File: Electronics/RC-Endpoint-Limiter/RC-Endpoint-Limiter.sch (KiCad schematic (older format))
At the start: 38 parts

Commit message: polished electornics
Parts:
- added J2: Aux Low, symbol Connector_Generic:Conn_01x03
- added J3: Aux High, symbol Connector_Generic:Conn_01x03
- added R7: 1K, symbol Device:R_Small
- added R8: 100R, symbol Device:R_Small
- R5: renamed from R?; value 240R -> 100R
- gave numbers to parts that had none: 37
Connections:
- net GND: now also J2.2 (Pin_2), J3.2 (Pin_2)
- net VCC: now also J2.1 (Pin_1), J3.1 (Pin_1)
- net at U1.11 (PB3): no longer R4.2
- net at U1.19 (PD1): now also R6.2
- net at U1.20 (PD2): now also R7.2
- net at U1.21 (PD3): now also R8.2
- net at U1.25 (PD4): now also R9.2
- net at U1.28 (PB4): now also J2.3 (Pin_3); no longer R6.2
- net at U1.29 (PB5): now also J3.3 (Pin_3); no longer R9.2
- net at U1.30 (PB6): now also R4.2
- net at D7.2 (A), J7.2 (Pin_2): now also JP1.1 (A); no longer JP1.2 (B)
- net at J7.3 (Pin_3), R5.1: now also R8.1
- net at D6.2 (A), J6.2 (Pin_2): now also JP1.2 (B); no longer JP1.1 (A)
- net at J6.3 (Pin_3), R9.1: now also R7.1
- no-connect marks 0 -> 15
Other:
- moved on the sheet: C1, C2, C3, C4, C5, C6, C7, D1, D2, D3, D4, D5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

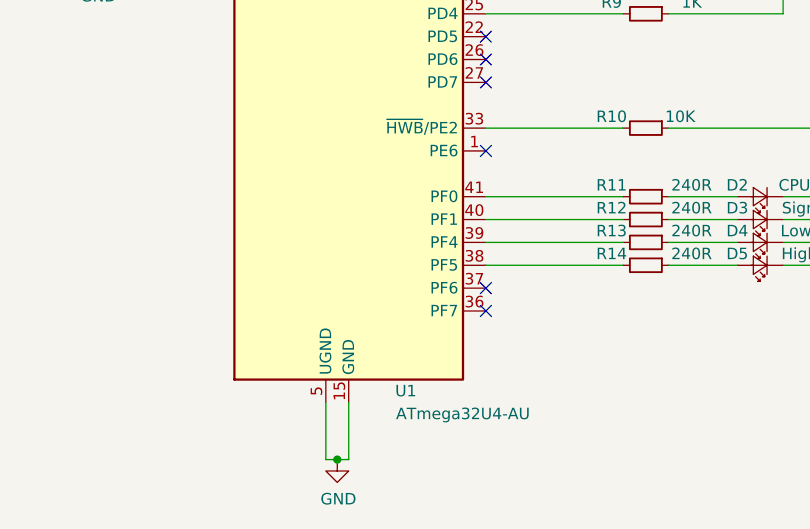
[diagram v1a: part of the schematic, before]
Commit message: started component assignment
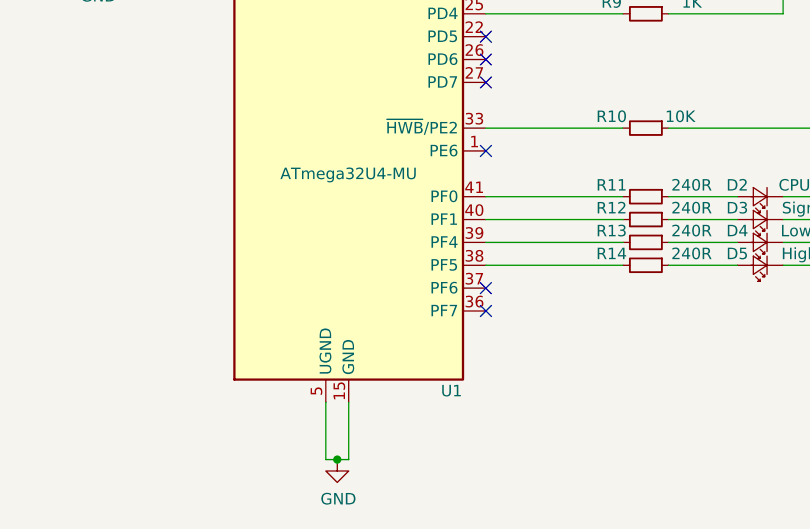
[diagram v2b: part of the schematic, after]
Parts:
- removed U1: ATmega32U4-AU, Package_QFP:TQFP-44_10x10mm_P0.8mm, symbol MCU_Microchip_ATmega:ATmega32U4-AU
- added U1: ATmega32U4-MU, Package_DFN_QFN:QFN-44-1EP_7x7mm_P0.5mm_EP5.2x5.2mm, symbol MCU_Microchip_ATmega:ATmega32U4-MU
- C1, C2, C3, C4, C5, C6, C7, R1, R10, R11, R12, R13, R14, R15, R16, R17, R18, R2, R3, R4, R5, R6, R7, R8, R9: footprint (none) -> Capacitor_SMD:C_0805_2012Metric
- J4, J5: footprint (none) -> Connector_AMASS:AMASS_MR30PW-FB_1x03_P3.50mm_Horizontal
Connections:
- net GND: now also U1.15 (GND), U1.23 (GND), U1.35 (GND), U1.43 (GND), U1.45 (GND), U1.5 (UGND)
- net VCC: now also U1.14 (VCC), U1.2 (UVCC), U1.24 (AVCC), U1.34 (VCC), U1.44 (AVCC)
- net at R3.1: now also U1.13 (~RESET)
- net at C2.2, Y1.2: now also U1.16 (XTAL2)
- net at C1.1, Y1.1: now also U1.17 (XTAL1)
- net at R6.2: now also U1.19 (PD1)
- net at R7.2: now also U1.20 (PD2)
- net at R8.2: now also U1.21 (PD3)
- net at R9.2: now also U1.25 (PD4)
- net at J2.3 (Pin_3): now also U1.28 (PB4)
- net at J3.3 (Pin_3): now also U1.29 (PB5)
- net at R2.1: now also U1.3 (D-)
- net at R4.2: now also U1.30 (PB6)
- net at R5.2: now also U1.31 (PC6)
- net at R10.2: now also U1.33 (~HWB~/PE2)
- net at R14.2: now also U1.38 (PF5)
- net at R13.2: now also U1.39 (PF4)
- net at R1.1: now also U1.4 (D+)
- net at R12.2: now also U1.40 (PF1)
- net at R11.2: now also U1.41 (PF0)
- net at C3.1: now also U1.42 (AREF)
- net at C4.1: now also U1.6 (UCAP)
- net at D1.2 (A), J1.1 (VBUS): now also U1.7 (VBUS)
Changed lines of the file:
@@
 EESchema Schematic File Version 4
 LIBS:RC-Endpoint-Limiter-cache
-EELAYER 30 0
+EELAYER 29 0
 EELAYER END
 $Descr A4 11693 8268
 encoding utf-8
 Sheet 1 1
-Title ""
-Date ""
-Rev ""
-Comp ""
+Title "RC Endpoint Limiter"
+Date "2019-09-01"
+Rev "0.01"
+Comp "Vapourforge"
 Comment1 ""
 Comment2 ""
@@
 F 0 "C1" V 2700 3000 50  0000 C CNN
 F 1 "22pf" V 2700 3300 50  0000 C CNN
-F 2 "" H 2750 3100 50  0001 C CNN
+F 2 "Capacitor_SMD:C_0805_2012Metric" H 2750 3100 50  0001 C CNN
 F 3 "~" H 2750 3100 50  0001 C CNN
 	1    2750 3100
@@
 F 0 "C2" V 2800 3400 50  0000 C CNN
 F 1 "22pf" V 2800 3100 50  0000 C CNN
-F 2 "" H 2750 3300 50  0001 C CNN
+F 2 "Capacitor_SMD:C_0805_2012Metric" H 2750 3300 50  0001 C CNN
 F 3 "~" H 2750 3300 50  0001 C CNN
 	1    2750 3300
@@
 F 0 "C3" V 2700 3400 50  0000 C CNN
 F 1 "100n" V 2700 3700 50  0000 C CNN
-F 2 "" H 2750 3500 50  0001 C CNN
+F 2 "Capacitor_SMD:C_0805_2012Metric" H 2750 3500 50  0001 C CNN
 F 3 "~" H 2750 3500 50  0001 C CNN
 	1    2750 3500
@@
 F 0 "R3" V 3150 2750 50  0000 C CNN
 F 1 "10K" V 3150 3050 50  0000 C CNN
-F 2 "" H 3200 2900 50  0001 C CNN
+F 2 "Capacitor_SMD:C_0805_2012Metric" H 3200 2900 50  0001 C CNN
 F 3 "~" H 3200 2900 50  0001 C CNN
 	1    3200 2900
@@
 F 0 "C7" V 4550 2350 50  0000 C CNN
 F 1 "1uF" V 4550 2650 50  0000 C CNN
-F 2 "" H 4600 2450 50  0001 C CNN
+F 2 "Capacitor_SMD:C_0805_2012Metric" H 4600 2450 50  0001 C CNN
 F 3 "~" H 4600 2450 50  0001 C CNN
 	1    4600 2450
@@
 F 0 "C6" V 4550 2200 50  0000 C CNN
 F 1 "1uF" V 4550 2500 50  0000 C CNN
-F 2 "" H 4600 2300 50  0001 C CNN
+F 2 "Capacitor_SMD:C_0805_2012Metric" H 4600 2300 50  0001 C CNN
 F 3 "~" H 4600 2300 50  0001 C CNN
 	1    4600 2300
@@
 F 0 "C5" V 4550 2050 50  0000 C CNN
 F 1 "1uF" V 4550 2350 50  0000 C CNN
-F 2 "" H 4600 2150 50  0001 C CNN
+F 2 "Capacitor_SMD:C_0805_2012Metric" H 4600 2150 50  0001 C CNN
 F 3 "~" H 4600 2150 50  0001 C CNN
 	1    4600 2150
@@
 F 0 "C4" V 3250 4100 50  0000 C CNN
 F 1 "1uF" V 3250 4400 50  0000 C CNN
-F 2 "" H 3300 4200 50  0001 C CNN
+F 2 "Capacitor_SMD:C_0805_2012Metric" H 3300 4200 50  0001 C CNN
 F 3 "~" H 3300 4200 50  0001 C CNN
 	1    3300 4200
@@
 F 0 "R1" V 2200 3750 50  0000 C CNN
 F 1 "22R" V 2200 4050 50  0000 C CNN
-F 2 "" H 2250 3900 50  0001 C CNN
+F 2 "Capacitor_SMD:C_0805_2012Metric" H 2250 3900 50  0001 C CNN
 F 3 "~" H 2250 3900 50  0001 C CNN
 	1    2250 3900
@@
 F 0 "R2" V 2200 3850 50  0000 C CNN
 F 1 "22R" V 2200 4150 50  0000 C CNN
-F 2 "" H 2250 4000 50  0001 C CNN
+F 2 "Capacitor_SMD:C_0805_2012Metric" H 2250 4000 50  0001 C CNN
 F 3 "~" H 2250 4000 50  0001 C CNN
 	1    2250 4000
@@
 F 0 "R11" V 5500 5150 50  0000 C CNN
 F 1 "240R" V 5500 5500 50  0000 C CNN
-F 2 "" H 5550 5300 50  0001 C CNN
+F 2 "Capacitor_SMD:C_0805_2012Metric" H 5550 5300 50  0001 C CNN
 F 3 "~" H 5550 5300 50  0001 C CNN
 	1    5550 5300
@@
 F 0 "R12" V 5500 5250 50  0000 C CNN
 F 1 "240R" V 5500 5600 50  0000 C CNN
-F 2 "" H 5550 5400 50  0001 C CNN
+F 2 "Capacitor_SMD:C_0805_2012Metric" H 5550 5400 50  0001 C CNN
 F 3 "~" H 5550 5400 50  0001 C CNN
 	1    5550 5400
@@
 F 0 "R13" V 5500 5350 50  0000 C CNN
 F 1 "240R" V 5500 5700 50  0000 C CNN
-F 2 "" H 5550 5500 50  0001 C CNN
+F 2 "Capacitor_SMD:C_0805_2012Metric" H 5550 5500 50  0001 C CNN
 F 3 "~" H 5550 5500 50  0001 C CNN
 	1    5550 5500
@@
 F 0 "R14" V 5500 5450 50  0000 C CNN
 F 1 "240R" V 5500 5800 50  0000 C CNN
-F 2 "" H 5550 5600 50  0001 C CNN
+F 2 "Capacitor_SMD:C_0805_2012Metric" H 5550 5600 50  0001 C CNN
 F 3 "~" H 5550 5600 50  0001 C CNN
 	1    5550 5600
@@
 F 0 "R10" V 5500 4850 50  0000 C CNN
 F 1 "10K" V 5500 5150 50  0000 C CNN
-F 2 "" H 5550 5000 50  0001 C CNN
+F 2 "Capacitor_SMD:C_0805_2012Metric" H 5550 5000 50  0001 C CNN
 F 3 "~" H 5550 5000 50  0001 C CNN
 	1    5550 5000
@@
 F 0 "J4" V 7288 2112 50  0000 R CNN
 F 1 "Switch Low" V 7400 2450 50  0000 R CNN
-F 2 "" H 7350 2300 50  0001 C CNN
+F 2 "Connector_AMASS:AMASS_MR30PW-FB_1x03_P3.50mm_Horizontal" H 7350 2300 50  0001 C CNN
 F 3 "~" H 7350 2300 50  0001 C CNN
 	1    7350 2300
@@
 F 0 "J5" V 8238 2112 50  0000 R CNN
 F 1 "Switch High" V 8350 2450 50  0000 R CNN
-F 2 "" H 8300 2300 50  0001 C CNN
+F 2 "Connector_AMASS:AMASS_MR30PW-FB_1x03_P3.50mm_Horizontal" H 8300 2300 50  0001 C CNN
 F 3 "~" H 8300 2300 50  0001 C CNN
 	1    8300 2300
@@
 F 0 "R15" V 7050 1750 50  0000 C CNN
 F 1 "240R" V 7050 2100 50  0000 C CNN
-F 2 "" H 7100 1900 50  0001 C CNN
+F 2 "Capacitor_SMD:C_0805_2012Metric" H 7100 1900 50  0001 C CNN
 F 3 "~" H 7100 1900 50  0001 C CNN
 	1    7100 1900
@@
 F 0 "R4" V 5500 3350 50  0000 C CNN
 F 1 "1K" V 5500 3700 50  0000 C CNN
-F 2 "" H 5550 3500 50  0001 C CNN
+F 2 "Capacitor_SMD:C_0805_2012Metric" H 5550 3500 50  0001 C CNN
 F 3 "~" H 5550 3500 50  0001 C CNN
 	1    5550 3500
@@
 F 0 "R6" V 5500 4050 50  0000 C CNN
 F 1 "1K" V 5500 4400 50  0000 C CNN
-F 2 "" H 5550 4200 50  0001 C CNN
+F 2 "Capacitor_SMD:C_0805_2012Metric" H 5550 4200 50  0001 C CNN
 F 3 "~" H 5550 4200 50  0001 C CNN
 	1    5550 4200
@@
 F 0 "R9" V 5500 4350 50  0000 C CNN
 F 1 "1K" V 5500 4700 50  0000 C CNN
-F 2 "" H 5550 4500 50  0001 C CNN
+F 2 "Capacitor_SMD:C_0805_2012Metric" H 5550 4500 50  0001 C CNN
 F 3 "~" H 5550 4500 50  0001 C CNN
 	1    5550 4500
@@
 F 0 "R5" V 5500 3650 50  0000 C CNN
 F 1 "100R" V 5500 4000 50  0000 C CNN
-F 2 "" H 5550 3800 50  0001 C CNN
+F 2 "Capacitor_SMD:C_0805_2012Metric" H 5550 3800 50  0001 C CNN
 F 3 "~" H 5550 3800 50  0001 C CNN
 	1    5550 3800
@@
 F 0 "R16" V 7650 2500 50  0000 C CNN
 F 1 "1K" V 7650 2850 50  0000 C CNN
-F 2 "" H 7700 2650 50  0001 C CNN
+F 2 "Capacitor_SMD:C_0805_2012Metric" H 7700 2650 50  0001 C CNN
 F 3 "~" H 7700 2650 50  0001 C CNN
 	1    7700 2650
@@
 F 0 "R18" V 8600 2500 50  0000 C CNN
 F 1 "1K" V 8600 2850 50  0000 C CNN
-F 2 "" H 8650 2650 50  0001 C CNN
+F 2 "Capacitor_SMD:C_0805_2012Metric" H 8650 2650 50  0001 C CNN
 F 3 "~" H 8650 2650 50  0001 C CNN
 	1    8650 2650
@@
 F 0 "R17" V 8000 1750 50  0000 C CNN
 F 1 "240R" V 8000 2100 50  0000 C CNN
-F 2 "" H 8050 1900 50  0001 C CNN
+F 2 "Capacitor_SMD:C_0805_2012Metric" H 8050 1900 50  0001 C CNN
 F 3 "~" H 8050 1900 50  0001 C CNN
 	1    8050 1900
@@
 F 0 "R8" V 5500 4250 50  0000 C CNN
 F 1 "100R" V 5500 4600 50  0000 C CNN
-F 2 "" H 5550 4400 50  0001 C CNN
+F 2 "Capacitor_SMD:C_0805_2012Metric" H 5550 4400 50  0001 C CNN
 F 3 "~" H 5550 4400 50  0001 C CNN
 	1    5550 4400
@@
 F 0 "R7" V 5500 4150 50  0000 C CNN
 F 1 "1K" V 5500 4500 50  0000 C CNN
-F 2 "" H 5550 4300 50  0001 C CNN
+F 2 "Capacitor_SMD:C_0805_2012Metric" H 5550 4300 50  0001 C CNN
 F 3 "~" H 5550 4300 50  0001 C CNN
 	1    5550 4300
@@
 Wire Wire Line
 	5650 3500 7450 3500
-$Comp
-L MCU_Microchip_ATmega:ATmega32U4-AU U1
-U 1 1 5D46E164
+NoConn ~ 4850 3200
+Wire Wire Line
+	6150 4300 10350 4300
+Wire Wire Line
+	9250 2000 9250 2150
+Wire Wire Line
+	9950 2000 9950 2150
+Wire Wire Line
+	9450 2150 9250 2150
+Connection ~ 9250 2150
+Wire Wire Line
+	9250 2150 9250 3000
+Wire Wire Line
+	9750 2150 9950 2150
+Connection ~ 9950 2150
+Wire Wire Line
+	9950 2150 9950 3000
+$Comp
+L MCU_Microchip_ATmega:ATmega32U4-MU U1
+U 1 1 5D6CC858
 P 4250 4400
-F 0 "U1" H 4500 2650 50  0000 C CNN
-F 1 "ATmega32U4-AU" H 4750 2550 50  0000 C CNN
-F 2 "Package_QFP:TQFP-44_10x10mm_P0.8mm" H 4250 4400 50  0001 C CIN
+F 0 "U1" H 4700 2650 50  0000 C CNN
+F 1 "ATmega32U4-MU" H 4250 3600 50  0000 C CNN
+F 2 "Package_DFN_QFN:QFN-44-1EP_7x7mm_P0.5mm_EP5.2x5.2mm" H 4250 4400 50  0001 C CIN
 F 3 "http://ww1.microchip.com/downloads/en/DeviceDoc/Atmel-7766-8-bit-AVR-ATmega16U4-32U4_Datasheet.pdf" H 4250 4400 50  0001 C CNN
 	1    4250 4400
 	1    0    0    -1
 $EndComp
-NoConn ~ 4850 3200
-Wire Wire Line
-	6150 4300 10350 4300
-Wire Wire Line
-	9250 2000 9250 2150
-Wire Wire Line
-	9950 2000 9950 2150
-Wire Wire Line
-	9450 2150 9250 2150
-Connection ~ 9250 2150
-Wire Wire Line
-	9250 2150 9250 3000
-Wire Wire Line
-	9750 2150 9950 2150
-Connection ~ 9950 2150
-Wire Wire Line
-	9950 2150 9950 3000
 $EndSCHEMATC

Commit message: component allocation
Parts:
- D2, D3, D4, D5: footprint (none) -> LED_SMD:LED_0805_2012Metric
- J1: footprint (none) -> Connector_USB:USB_Micro-B_Amphenol_10103594-0001LF_Horizontal
- J2, J3, J6, J7: footprint (none) -> Connector_PinHeader_1.27mm:PinHeader_1x03_P1.27mm_Vertical
- JP1: footprint (none) -> Jumper:SolderJumper-2_P1.3mm_Open_Pad1.0x1.5mm
- Y1: footprint (none) -> Crystal:Crystal_SMD_5032-4Pin_5.0x3.2mm
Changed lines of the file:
@@
 F 0 "Y1" V 3154 3288 50  0000 L CNN
 F 1 "8Mhz" V 3245 3288 50  0000 L CNN
-F 2 "" H 3200 3200 50  0001 C CNN
+F 2 "Crystal:Crystal_SMD_5032-4Pin_5.0x3.2mm" H 3200 3200 50  0001 C CNN
 F 3 "~" H 3200 3200 50  0001 C CNN
 	1    3200 3200
@@
 F 0 "J1" H 1607 4367 50  0000 C CNN
 F 1 "USB_B_Micro" H 1607 4276 50  0000 C CNN
-F 2 "" H 1700 3850 50  0001 C CNN
+F 2 "Connector_USB:USB_Micro-B_Amphenol_10103594-0001LF_Horizontal" H 1700 3850 50  0001 C CNN
 F 3 "~" H 1700 3850 50  0001 C CNN
 	1    1550 3900
@@
 F 0 "D2" H 6150 5250 50  0000 C CNN
 F 1 "CPU" H 5900 5250 50  0000 C CNN
-F 2 "" V 6050 5300 50  0001 C CNN
+F 2 "LED_SMD:LED_0805_2012Metric" V 6050 5300 50  0001 C CNN
 F 3 "~" V 6050 5300 50  0001 C CNN
 	1    6050 5300
@@
 F 0 "D3" H 6150 5350 50  0000 C CNN
 F 1 "Signal" H 5850 5350 50  0000 C CNN
-F 2 "" V 6050 5400 50  0001 C CNN
+F 2 "LED_SMD:LED_0805_2012Metric" V 6050 5400 50  0001 C CNN
 F 3 "~" V 6050 5400 50  0001 C CNN
 	1    6050 5400
@@
 F 0 "D4" H 6150 5450 50  0000 C CNN
 F 1 "Low" H 5825 5450 50  0000 L CNN
-F 2 "" V 6050 5500 50  0001 C CNN
+F 2 "LED_SMD:LED_0805_2012Metric" V 6050 5500 50  0001 C CNN
 F 3 "~" V 6050 5500 50  0001 C CNN
 	1    6050 5500
@@
 F 0 "D5" H 6150 5550 50  0000 C CNN
 F 1 "High" H 5800 5550 50  0000 L CNN
-F 2 "" V 6050 5600 50  0001 C CNN
+F 2 "LED_SMD:LED_0805_2012Metric" V 6050 5600 50  0001 C CNN
 F 3 "~" V 6050 5600 50  0001 C CNN
 	1    6050 5600
@@
 F 0 "J7" V 9514 2262 50  0000 R CNN
 F 1 "RC Output" V 9700 2600 50  0000 R CNN
-F 2 "" H 9550 2450 50  0001 C CNN
+F 2 "Connector_PinHeader_1.27mm:PinHeader_1x03_P1.27mm_Vertical" H 9550 2450 50  0001 C CNN
 F 3 "~" H 9550 2450 50  0001 C CNN
 	1    9550 2450
@@
 F 0 "J6" V 10214 2262 50  0000 R CNN
 F 1 "RC Input" V 10400 2600 50  0000 R CNN
-F 2 "" H 10250 2450 50  0001 C CNN
+F 2 "Connector_PinHeader_1.27mm:PinHeader_1x03_P1.27mm_Vertical" H 10250 2450 50  0001 C CNN
 F 3 "~" H 10250 2450 50  0001 C CNN
 	1    10250 2450
@@
 F 0 "JP1" H 9600 2355 50  0000 C CNN
 F 1 "PassThrough" H 9600 2264 50  0000 C CNN
-F 2 "" H 9600 2150 50  0001 C CNN
+F 2 "Jumper:SolderJumper-2_P1.3mm_Open_Pad1.0x1.5mm" H 9600 2150 50  0001 C CNN
 F 3 "~" H 9600 2150 50  0001 C CNN
 	1    9600 2150
@@
 F 0 "J2" V 6014 2262 50  0000 R CNN
 F 1 "Aux Low" V 6200 2600 50  0000 R CNN
-F 2 "" H 6050 2450 50  0001 C CNN
+F 2 "Connector_PinHeader_1.27mm:PinHeader_1x03_P1.27mm_Vertical" H 6050 2450 50  0001 C CNN
 F 3 "~" H 6050 2450 50  0001 C CNN
 	1    6050 2450
@@
 F 0 "J3" V 6614 2262 50  0000 R CNN
 F 1 "Aux High" V 6800 2600 50  0000 R CNN
-F 2 "" H 6650 2450 50  0001 C CNN
+F 2 "Connector_PinHeader_1.27mm:PinHeader_1x03_P1.27mm_Vertical" H 6650 2450 50  0001 C CNN
 F 3 "~" H 6650 2450 50  0001 C CNN
 	1    6650 2450

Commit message: first draft PCB
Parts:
- added J8: Inhibit Input, Connector_PinHeader_1.27mm:PinHeader_1x03_P1.27mm_Horizontal, symbol Connector_Generic:Conn_01x03
- added R19: 1K, Resistor_SMD:R_0603_1608Metric, symbol Device:R_Small
- C1, C2, C3, C4, C5, C6, C7: footprint Capacitor_SMD:C_0805_2012Metric -> Capacitor_SMD:C_0603_1608Metric
- D1, D6, D7: footprint (none) -> Diode_SMD:D_SMA
- D2, D3, D4, D5: footprint LED_SMD:LED_0805_2012Metric -> LED_SMD:LED_0603_1608Metric
- J2, J3, J6, J7: footprint Connector_PinHeader_1.27mm:PinHeader_1x03_P1.27mm_Vertical -> Connector_PinHeader_1.27mm:PinHeader_1x03_P1.27mm_Horizontal
- J4, J5: footprint Connector_AMASS:AMASS_MR30PW-FB_1x03_P3.50mm_Horizontal -> Connector_AMASS:AMASS_XT30PW-F_1x02_P2.50mm_Horizontal
- R1, R10, R11, R12, R13, R14, R15, R16, R17, R18, R2, R3, R4, R5, R6, R7, R8, R9: footprint Capacitor_SMD:C_0805_2012Metric -> Resistor_SMD:R_0603_1608Metric
- Y1: footprint Crystal:Crystal_SMD_5032-4Pin_5.0x3.2mm -> Crystal:Crystal_SMD_5032-2Pin_5.0x3.2mm
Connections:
- net GND: now also J8.1 (Pin_1)
- net at U1.11 (PB3): now also R19.2
- new net: J8.3 (Pin_3), R19.1
- no-connect marks 15 -> 14
